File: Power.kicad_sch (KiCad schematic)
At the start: 34 parts, among them J1 12V, Q1 ZVP2106GTA, U1 TPS7A2633DRVR, U2 TPS54202DDC, U3 TPS7A2633DRVR

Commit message: refactored project
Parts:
- removed D1: D_Zener, Diode_SMD:D_SMA_Handsoldering, symbol Device:D_Zener
- removed Q1: ZVP2106GTA, Package_TO_SOT_SMD:SOT-223-3_TabPin2, symbol Simulation_SPICE:PMOS
- removed R1: 10K, Resistor_SMD:R_0402_1005Metric_Pad0.72x0.64mm_HandSolder, symbol Device:R
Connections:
- net +12V: now also J1.1 (Pin_1)
- net SW: no longer names the net of C5.2, L1.1, U2.2 (SW)
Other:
- moved on the sheet: J1

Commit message: [Fix] Schematic and layout. - Replaced STM32WLE5x symbol for better visualization of the symbols - Added some missing connections - Modified some components' values - Changed the layout for STM32WL
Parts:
- C1, C10, C6, C9: footprint Capacitor_SMD:C_0805_2012Metric_Pad1.18x1.45mm_HandSolder -> Capacitor_SMD:C_0805_2012Metric
- C2, C7, C8: footprint Capacitor_SMD:C_1206_3216Metric_Pad1.33x1.80mm_HandSolder -> Capacitor_SMD:C_1206_3216Metric
- C3: footprint Capacitor_SMD:C_0603_1608Metric -> Capacitor_SMD:C_0402_1005Metric
- C4, C5: footprint Capacitor_SMD:C_0402_1005Metric_Pad0.74x0.62mm_HandSolder -> Capacitor_SMD:C_0402_1005Metric
- R10, R11, R12, R13, R14, R2, R3, R4, R5, R6, R7, R8, R9: footprint Resistor_SMD:R_0402_1005Metric_Pad0.72x0.64mm_HandSolder -> Resistor_SMD:R_0402_1005Metric

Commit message: update problem
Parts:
- renumbered D2 to D1, D3 to D2, D4 to D3, R2 to R1, R11 to R10, R12 to R11, R13 to R12, R14 to R13, R3 to R2, R4 to R3, R5 to R4, R6 to R5, R7 to R6, R8 to R7, R9 to R8, R10 to R9
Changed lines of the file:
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@@
 		(dnp no)
 		(fields_autoplaced yes)
-		(property "Reference" "R10"
+		(property "Reference" "R9"
 			(at 168.91 92.7099 0)
 			(effects
@@
 			(project "airlora-kicad"
 				(path "/59d971df-d6c1-4ef7-a085-bf08b7b16047/be77b740-d58b-414b-97ce-61f1d1685314/af8bb3f5-67b6-4471-83fd-9297b14489a9"
-					(reference "R10")
+					(reference "R9")
 					(unit 1)
 				)
@@
 		(dnp no)
 		(fields_autoplaced yes)
-		(property "Reference" "D2"
+		(property "Reference" "D1"
 			(at 149.86 127.3174 90)
 			(effects
@@
 			(project "airlora-kicad"
 				(path "/59d971df-d6c1-4ef7-a085-bf08b7b16047/be77b740-d58b-414b-97ce-61f1d1685314/af8bb3f5-67b6-4471-83fd-9297b14489a9"
-					(reference "D2")
+					(reference "D1")
 					(unit 1)
 				)
@@
 		(on_board yes)
 		(dnp no)
-		(property "Reference" "R6"
+		(property "Reference" "R5"
 			(at 136.144 82.55 0)
 			(effects
@@
 			(project "airlora-kicad"
 				(path "/59d971df-d6c1-4ef7-a085-bf08b7b16047/be77b740-d58b-414b-97ce-61f1d1685314/af8bb3f5-67b6-4471-83fd-9297b14489a9"
-					(reference "R6")
+					(reference "R5")
 					(unit 1)
 				)
@@
 		(dnp no)
 		(fields_autoplaced yes)
-		(property "Reference" "R14"
+		(property "Reference" "R13"
 			(at 276.86 95.2499 0)
 			(effects
@@
 			(project "airlora-kicad"
 				(path "/59d971df-d6c1-4ef7-a085-bf08b7b16047/be77b740-d58b-414b-97ce-61f1d1685314/af8bb3f5-67b6-4471-83fd-9297b14489a9"
-					(reference "R14")
+					(reference "R13")
 					(unit 1)
 				)
@@
 		(dnp no)
 		(fields_autoplaced yes)
-		(property "Reference" "R5"
+		(property "Reference" "R4"
 			(at 128.27 134.6199 0)
 			(effects
@@
 			(project "airlora-kicad"
 				(path "/59d971df-d6c1-4ef7-a085-bf08b7b16047/be77b740-d58b-414b-97ce-61f1d1685314/af8bb3f5-67b6-4471-83fd-9297b14489a9"
-					(reference "R5")
+					(reference "R4")
 					(unit 1)
 				)
@@
 		(dnp no)
 		(fields_autoplaced yes)
-		(property "Reference" "R13"
+		(property "Reference" "R12"
 			(at 256.54 92.7099 0)
 			(effects
@@
 			(project "airlora-kicad"
 				(path "/59d971df-d6c1-4ef7-a085-bf08b7b16047/be77b740-d58b-414b-97ce-61f1d1685314/af8bb3f5-67b6-4471-83fd-9297b14489a9"
-					(reference "R13")
+					(reference "R12")
 					(unit 1)
 				)
@@
 		(dnp no)
 		(fields_autoplaced yes)
-		(property "Reference" "R12"
+		(property "Reference" "R11"
 			(at 256.54 82.5499 0)
 			(effects
@@
 			(project "airlora-kicad"
 				(path "/59d971df-d6c1-4ef7-a085-bf08b7b16047/be77b740-d58b-414b-97ce-61f1d1685314/af8bb3f5-67b6-4471-83fd-9297b14489a9"
-					(reference "R12")
+					(reference "R11")
 					(unit 1)
 				)
@@
 		(dnp no)
 		(fields_autoplaced yes)
-		(property "Reference" "R9"
+		(property "Reference" "R8"
 			(at 148.59 137.1599 0)
 			(effects
@@
 			(project "airlora-kicad"
 				(path "/59d971df-d6c1-4ef7-a085-bf08b7b16047/be77b740-d58b-414b-97ce-61f1d1685314/af8bb3f5-67b6-4471-83fd-9297b14489a9"
-					(reference "R9")
+					(reference "R8")
 					(unit 1)
 				)
@@
 		(on_board yes)
 		(dnp no)
-		(property "Reference" "R2"
+		(property "Reference" "R1"
 			(at 102.87 86.36 0)
 			(effects
@@
 			(project "airlora-kicad"
 				(path "/59d971df-d6c1-4ef7-a085-bf08b7b16047/be77b740-d58b-414b-97ce-61f1d1685314/af8bb3f5-67b6-4471-83fd-9297b14489a9"
-					(reference "R2")
+					(reference "R1")
 					(unit 1)
 				)
@@
 		(on_board yes)
 		(dnp no)
-		(property "Reference" "R7"
+		(property "Reference" "R6"
 			(at 135.89 91.44 0)
 			(effects
@@
 			(project "airlora-kicad"
 				(path "/59d971df-d6c1-4ef7-a085-bf08b7b16047/be77b740-d58b-414b-97ce-61f1d1685314/af8bb3f5-67b6-4471-83fd-9297b14489a9"
-					(reference "R7")
+					(reference "R6")
 					(unit 1)
 				)
@@
 		(dnp no)
 		(fields_autoplaced yes)
-		(property "Reference" "D4"
+		(property "Reference" "D3"
 			(at 278.13 85.4074 90)
 			(effects
@@
 			(project "airlora-kicad"
 				(path "/59d971df-d6c1-4ef7-a085-bf08b7b16047/be77b740-d58b-414b-97ce-61f1d1685314/af8bb3f5-67b6-4471-83fd-9297b14489a9"
-					(reference "D4")
+					(reference "D3")
 					(unit 1)
 				)
@@
 		(on_board yes)
 		(dnp no)
-		(property "Reference" "R11"
+		(property "Reference" "R10"
 			(at 243.84 81.28 90)
 			(effects
@@
 			(project "airlora-kicad"
 				(path "/59d971df-d6c1-4ef7-a085-bf08b7b16047/be77b740-d58b-414b-97ce-61f1d1685314/af8bb3f5-67b6-4471-83fd-9297b14489a9"
-					(reference "R11")
+					(reference "R10")
 					(unit 1)
 				)
@@
 		(dnp no)
 		(fields_autoplaced yes)
-		(property "Reference" "D3"
+		(property "Reference" "D2"
 			(at 170.18 82.8674 90)
 			(effects
@@
 			(project "airlora-kicad"
 				(path "/59d971df-d6c1-4ef7-a085-bf08b7b16047/be77b740-d58b-414b-97ce-61f1d1685314/af8bb3f5-67b6-4471-83fd-9297b14489a9"
-					(reference "D3")
+					(reference "D2")
 					(unit 1)
 				)
@@
 		(on_board yes)
 		(dnp no)
-		(property "Reference" "R8"
+		(property "Reference" "R7"
 			(at 143.51 82.55 0)
 			(effects
@@
 			(project "airlora-kicad"
 				(path "/59d971df-d6c1-4ef7-a085-bf08b7b16047/be77b740-d58b-414b-97ce-61f1d1685314/af8bb3f5-67b6-4471-83fd-9297b14489a9"
-					(reference "R8")
+					(reference "R7")
 					(unit 1)
 				)
@@
 		(dnp no)
 		(fields_autoplaced yes)
-		(property "Reference" "R4"
+		(property "Reference" "R3"
 			(at 128.27 124.4599 0)
 			(effects
@@
 			(project "airlora-kicad"
 				(path "/59d971df-d6c1-4ef7-a085-bf08b7b16047/be77b740-d58b-414b-97ce-61f1d1685314/af8bb3f5-67b6-4471-83fd-9297b14489a9"
-					(reference "R4")
+					(reference "R3")
 					(unit 1)
 				)
@@
 		(on_board yes)
 		(dnp no)
-		(property "Reference" "R3"
+		(property "Reference" "R2"
 			(at 115.57 123.19 90)
 			(effects
@@
 			(project "airlora-kicad"
 				(path "/59d971df-d6c1-4ef7-a085-bf08b7b16047/be77b740-d58b-414b-97ce-61f1d1685314/af8bb3f5-67b6-4471-83fd-9297b14489a9"
-					(reference "R3")
+					(reference "R2")
 					(unit 1)
 				)

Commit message: Update schematic
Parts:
- removed C10, C9: 1uF, Capacitor_SMD:C_0805_2012Metric, symbol Device:C
- removed D3: LED, LED_SMD:LED_0603_1608Metric_Pad1.05x0.95mm_HandSolder, symbol Device:LED
- removed R10: 10K, Resistor_SMD:R_0402_1005Metric, symbol Device:R
- removed R11: 1.96M, Resistor_SMD:R_0402_1005Metric, symbol Device:R
- removed R12: 1.18M, Resistor_SMD:R_0402_1005Metric, symbol Device:R
- removed R13: 1k, Resistor_SMD:R_0402_1005Metric, symbol Device:R
- removed U3: TPS7A2633DRVR, footprint:TPS7A2633DRVR, symbol TPS7A2633DRVR:TPS7A2633DRVR
- added J11, J14, J15: Conn_01x02_Pin, symbol Connector:Conn_01x02_Pin
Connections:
- net +12V: now also J11.2 (Pin_2); no longer J1.1 (Pin_1)
- net +3.3V: now also J15.2 (Pin_2)
- net +5V: now also J14.2 (Pin_2); no longer C7.1, C8.1, D2.2 (A), L1.2, R7.2
- net +3.3V_HP: no longer names the net of C6.1, D1.2 (A), R2.2, R3.1, U1.1 (OUT)
- net +3.3V_HP: now also J15.1 (Pin_1)
- new net: C7.1, C8.1, D2.2 (A), J14.1 (Pin_1), L1.2, R7.2
- new net: J1.1 (Pin_1), J11.1 (Pin_1)
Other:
- note removed: "Relglutlor 12V - 3.3V"
- moved on the sheet: C1, C2, C3, C4, C5, C6, C7, C8, D1, D2, J1, L1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

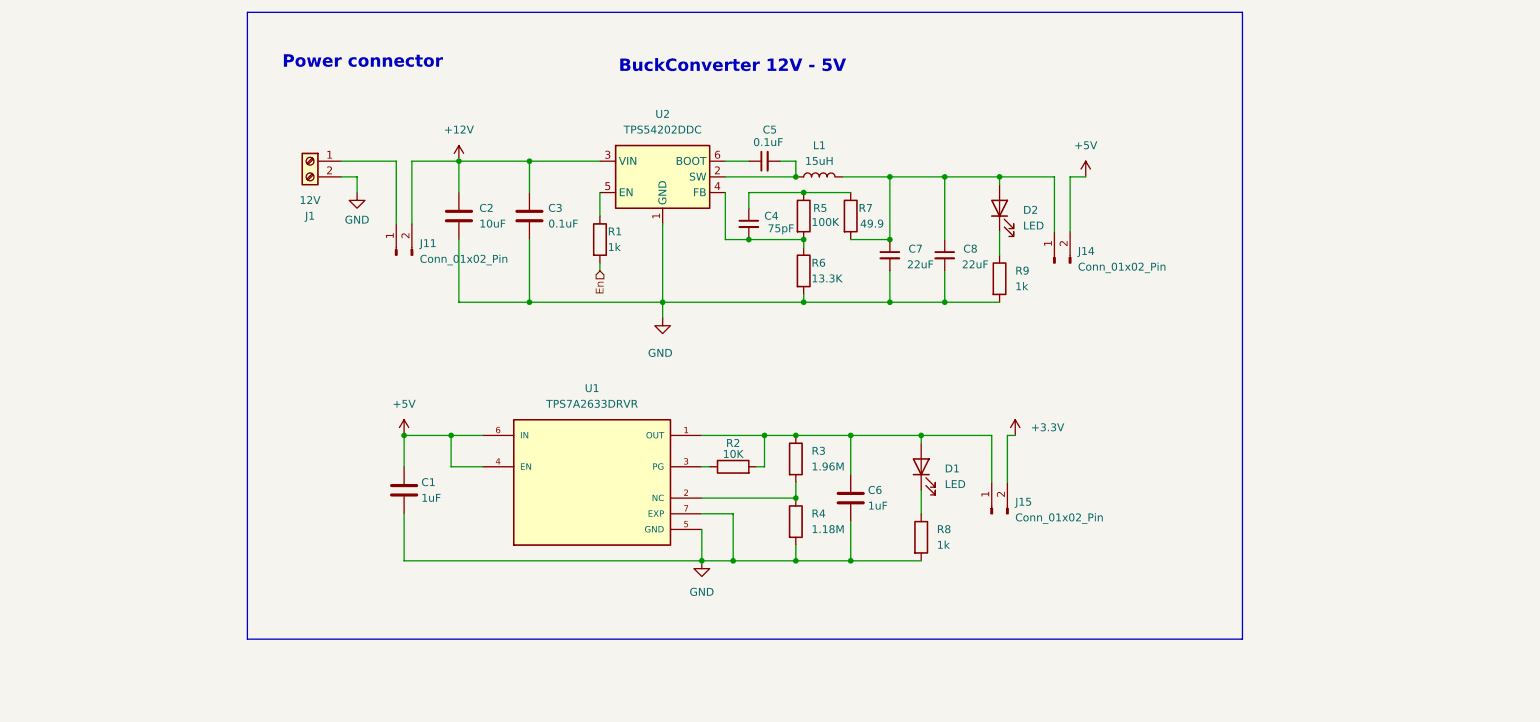
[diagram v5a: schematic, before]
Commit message: Udpate test point
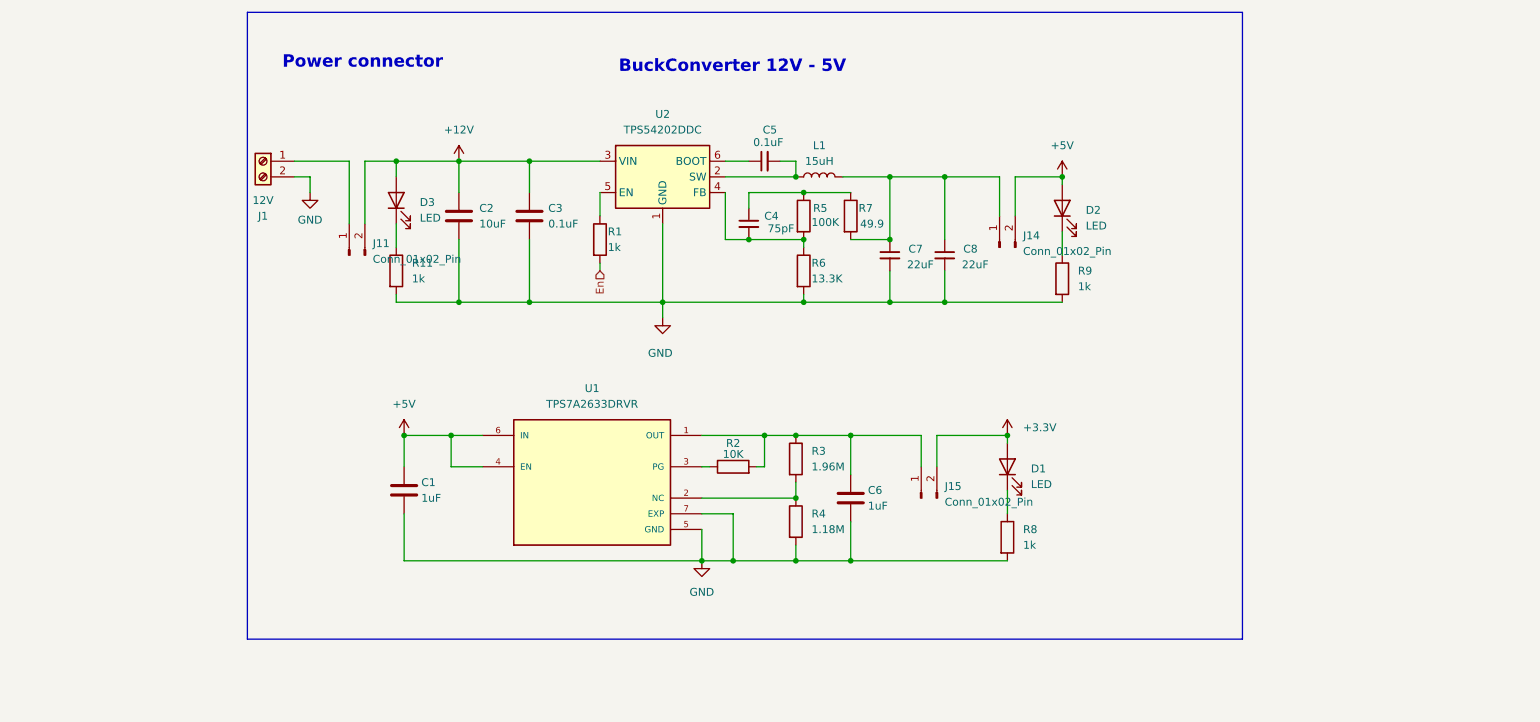
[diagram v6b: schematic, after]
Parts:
- added D3: LED, LED_SMD:LED_0603_1608Metric_Pad1.05x0.95mm_HandSolder, symbol Device:LED
- added R11: 1k, Resistor_SMD:R_0402_1005Metric, symbol Device:R
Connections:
- net +12V: now also D3.2 (A)
- net +3.3V: now also D1.2 (A)
- net +5V: now also D2.2 (A)
- net GND: now also R11.2
- net at C7.1, C8.1, J14.1 (Pin_1)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: no longer D2.2 (A)
- net at C6.1, J15.1 (Pin_1), R2.2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: no longer D1.2 (A)
- new net: D3.1 (K), R11.1
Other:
- moved on the sheet: D1, D2, J1, J11, J14, J15, R8, R9

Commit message: Update schemtic
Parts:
- R11: value 1k -> 3k
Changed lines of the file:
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@@
 			)
 		)
-		(property "Value" "1k"
+		(property "Value" "3k"
 			(at 101.6 85.0899 0)
 			(effects

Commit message: Update PCB layout
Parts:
- C3: footprint Capacitor_SMD:C_0402_1005Metric -> Capacitor_SMD:C_0603_1608Metric
- J11, J14, J15: footprint (none) -> Connector_PinHeader_2.54mm:PinHeader_1x02_P2.54mm_Vertical
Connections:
- net a: now reaches C7.1, C8.1, J14.1 (Pin_1), L1.2, R7.2
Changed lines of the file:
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@@
 	(wire
 		(pts
+			(xy 179.07 64.77) (xy 179.07 68.58)
+		)
+		(stroke
+			(width 0)
+			(type default)
+		)
+	)
+	(wire
+		(pts
 			(xy 179.07 68.58) (xy 187.96 68.58)
 		)
@@
 		)
 	)
+	(global_label "a"
+		(shape input)
+		(at 179.07 64.77 0)
+		(fields_autoplaced yes)
+		(effects
+			(font
+				(size 1.27 1.27)
+			)
+			(justify left)
+		)
+		(property "Intersheetrefs" "${INTERSHEET_REFS}"
+			(at 183.2042 64.77 0)
+			(effects
+				(font
+					(size 1.27 1.27)
+				)
+				(justify left)
+				(hide yes)
+			)
+		)
+	)
 	(hierarchical_label "En"
 		(shape input)
@@
 			)
 		)
-		(property "Footprint" ""
+		(property "Footprint" "Connector_PinHeader_2.54mm:PinHeader_1x02_P2.54mm_Vertical"
 			(at 184.15 120.65 0)
 			(effects
@@
 			)
 		)
-		(property "Footprint" ""
+		(property "Footprint" "Connector_PinHeader_2.54mm:PinHeader_1x02_P2.54mm_Vertical"
 			(at 91.44 81.28 0)
 			(effects
@@
 			)
 		)
-		(property "Footprint" ""
+		(property "Footprint" "Connector_PinHeader_2.54mm:PinHeader_1x02_P2.54mm_Vertical"
 			(at 196.85 80.01 0)
 			(effects
@@
 			)
 		)
-		(property "Footprint" "Capacitor_SMD:C_0402_1005Metric"
+		(property "Footprint" "Capacitor_SMD:C_0603_1608Metric"
 			(at 121.6152 78.74 0)
 			(effects
